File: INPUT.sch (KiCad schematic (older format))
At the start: 41 parts, among them Q701 MMBF170, SW701 SW_PUSH, SW702 C, SW703 1, SW704 4ghi, SW705 7pqrs, SW706 -, SW707 2abc, SW708 5jkl, SW709 8tuv, SW710 UP, SW711 3def, SW712 6mno, SW713 9wxyz, SW714 *+, SW715 DOWN, SW716 0space, SW717 #up

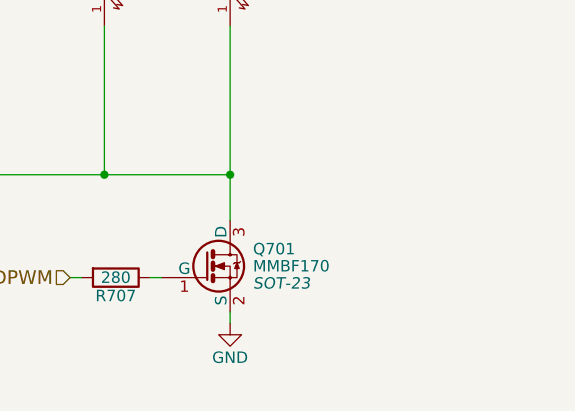
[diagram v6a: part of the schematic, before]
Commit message: Created netlist with current components Foreward Annotation to Board
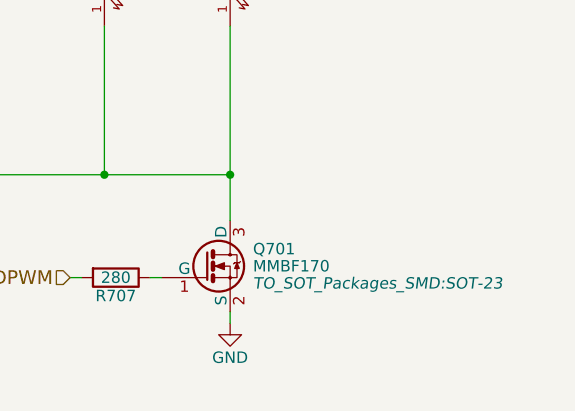
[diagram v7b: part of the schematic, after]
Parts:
- D701, D702, D703, D704, D705, D706: footprint (none) -> LEDs:LED_0603
- Q701: footprint SOT-23 -> TO_SOT_Packages_SMD:SOT-23
- R701, R702, R703, R704, R705, R706, R707, R708: footprint Resistors_SMD:R_0603 -> Resistors_SMD:R_0402
- SW701: footprint buttons:TS-015A -> NokiaRetroFit:TS-015A
- SW702, SW703, SW704, SW705, SW706, SW707, SW708, SW709, SW710, SW711, SW712, SW713, SW714, SW715, SW716, SW717: footprint buttons:Foil_Button -> NokiaRetroFit:Foil_Button
- TP701, TP702, TP703, TP704, TP705, TP706, TP707, TP708, TP709: footprint buttons:TP -> NokiaRetroFit:TP
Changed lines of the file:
@@
 F 0 "SW702" H 2950 3110 50  0000 C CNN
 F 1 "C" H 2800 2921 50  0000 C CNN
-F 2 "buttons:Foil_Button" H 2800 3000 50  0001 C CNN
+F 2 "NokiaRetroFit:Foil_Button" H 2800 3000 50  0001 C CNN
 F 3 "" H 2800 3000 50  0000 C CNN
 	1    2800 3000
@@
 F 0 "SW706" H 3500 3110 50  0000 C CNN
 F 1 "-" H 3350 2921 50  0000 C CNN
-F 2 "buttons:Foil_Button" H 3350 3000 50  0001 C CNN
+F 2 "NokiaRetroFit:Foil_Button" H 3350 3000 50  0001 C CNN
 F 3 "" H 3350 3000 50  0000 C CNN
 	1    3350 3000
@@
 F 0 "SW710" H 4050 3110 50  0000 C CNN
 F 1 "UP" H 3900 2921 50  0000 C CNN
-F 2 "buttons:Foil_Button" H 3900 3000 50  0001 C CNN
+F 2 "NokiaRetroFit:Foil_Button" H 3900 3000 50  0001 C CNN
 F 3 "" H 3900 3000 50  0000 C CNN
 	1    3900 3000
@@
 F 0 "SW715" H 4600 3710 50  0000 C CNN
 F 1 "DOWN" H 4450 3521 50  0000 C CNN
-F 2 "buttons:Foil_Button" H 4450 3600 50  0001 C CNN
+F 2 "NokiaRetroFit:Foil_Button" H 4450 3600 50  0001 C CNN
 F 3 "" H 4450 3600 50  0000 C CNN
 	1    4450 3600
@@
 F 0 "SW703" H 2950 3710 50  0000 C CNN
 F 1 "1" H 2800 3521 50  0000 C CNN
-F 2 "buttons:Foil_Button" H 2800 3600 50  0001 C CNN
+F 2 "NokiaRetroFit:Foil_Button" H 2800 3600 50  0001 C CNN
 F 3 "" H 2800 3600 50  0000 C CNN
 	1    2800 3600
@@
 F 0 "SW707" H 3500 3710 50  0000 C CNN
 F 1 "2abc" H 3350 3521 50  0000 C CNN
-F 2 "buttons:Foil_Button" H 3350 3600 50  0001 C CNN
+F 2 "NokiaRetroFit:Foil_Button" H 3350 3600 50  0001 C CNN
 F 3 "" H 3350 3600 50  0000 C CNN
 	1    3350 3600
@@
 F 0 "SW711" H 4050 3710 50  0000 C CNN
 F 1 "3def" H 3900 3521 50  0000 C CNN
-F 2 "buttons:Foil_Button" H 3900 3600 50  0001 C CNN
+F 2 "NokiaRetroFit:Foil_Button" H 3900 3600 50  0001 C CNN
 F 3 "" H 3900 3600 50  0000 C CNN
 	1    3900 3600
@@
 F 0 "SW704" H 2950 4310 50  0000 C CNN
 F 1 "4ghi" H 2800 4121 50  0000 C CNN
-F 2 "buttons:Foil_Button" H 2800 4200 50  0001 C CNN
+F 2 "NokiaRetroFit:Foil_Button" H 2800 4200 50  0001 C CNN
 F 3 "" H 2800 4200 50  0000 C CNN
 	1    2800 4200
@@
 F 0 "SW708" H 3500 4310 50  0000 C CNN
 F 1 "5jkl" H 3350 4121 50  0000 C CNN
-F 2 "buttons:Foil_Button" H 3350 4200 50  0001 C CNN
+F 2 "NokiaRetroFit:Foil_Button" H 3350 4200 50  0001 C CNN
 F 3 "" H 3350 4200 50  0000 C CNN
 	1    3350 4200
@@
 F 0 "SW712" H 4050 4310 50  0000 C CNN
 F 1 "6mno" H 3900 4121 50  0000 C CNN
-F 2 "buttons:Foil_Button" H 3900 4200 50  0001 C CNN
+F 2 "NokiaRetroFit:Foil_Button" H 3900 4200 50  0001 C CNN
 F 3 "" H 3900 4200 50  0000 C CNN
 	1    3900 4200
@@
 F 0 "SW705" H 2950 4910 50  0000 C CNN
 F 1 "7pqrs" H 2800 4721 50  0000 C CNN
-F 2 "buttons:Foil_Button" H 2800 4800 50  0001 C CNN
+F 2 "NokiaRetroFit:Foil_Button" H 2800 4800 50  0001 C CNN
 F 3 "" H 2800 4800 50  0000 C CNN
 	1    2800 4800
@@
 F 0 "SW709" H 3500 4910 50  0000 C CNN
 F 1 "8tuv" H 3350 4721 50  0000 C CNN
-F 2 "buttons:Foil_Button" H 3350 4800 50  0001 C CNN
+F 2 "NokiaRetroFit:Foil_Button" H 3350 4800 50  0001 C CNN
 F 3 "" H 3350 4800 50  0000 C CNN
 	1    3350 4800
@@
 F 0 "SW713" H 4050 4910 50  0000 C CNN
 F 1 "9wxyz" H 3900 4721 50  0000 C CNN
-F 2 "buttons:Foil_Button" H 3900 4800 50  0001 C CNN
+F 2 "NokiaRetroFit:Foil_Button" H 3900 4800 50  0001 C CNN
 F 3 "" H 3900 4800 50  0000 C CNN
 	1    3900 4800
@@
 F 0 "SW714" H 4600 3110 50  0000 C CNN
 F 1 "*+" H 4450 2921 50  0000 C CNN
-F 2 "buttons:Foil_Button" H 4450 3000 50  0001 C CNN
+F 2 "NokiaRetroFit:Foil_Button" H 4450 3000 50  0001 C CNN
 F 3 "" H 4450 3000 50  0000 C CNN
 	1    4450 3000
@@
 F 0 "SW716" H 4600 4310 50  0000 C CNN
 F 1 "0space" H 4450 4121 50  0000 C CNN
-F 2 "buttons:Foil_Button" H 4450 4200 50  0001 C CNN
+F 2 "NokiaRetroFit:Foil_Button" H 4450 4200 50  0001 C CNN
 F 3 "" H 4450 4200 50  0000 C CNN
 	1    4450 4200
@@
 F 0 "SW717" H 4600 4910 50  0000 C CNN
 F 1 "#up" H 4450 4721 50  0000 C CNN
-F 2 "buttons:Foil_Button" H 4450 4800 50  0001 C CNN
+F 2 "NokiaRetroFit:Foil_Button" H 4450 4800 50  0001 C CNN
 F 3 "" H 4450 4800 50  0000 C CNN
 	1    4450 4800
@@
 F 0 "SW701" H 1850 4510 50  0000 C CNN
 F 1 "SW_PUSH" H 1700 4320 50  0000 C CNN
-F 2 "buttons:TS-015A" H 1700 4400 50  0001 C CNN
+F 2 "NokiaRetroFit:TS-015A" H 1700 4400 50  0001 C CNN
 F 3 "" H 1700 4400 50  0000 C CNN
 	1    1700 4400
@@
 F 0 "R701" V 1780 3650 50  0000 C CNN
 F 1 "10k" V 1700 3650 50  0000 C CNN
-F 2 "Resistors_SMD:R_0603" V 1630 3650 50  0001 C CNN
+F 2 "Resistors_SMD:R_0402" V 1630 3650 50  0001 C CNN
 F 3 "" H 1700 3650 50  0000 C CNN
 	1    1700 3650
@@
 F 0 "R702" V 7130 2650 50  0000 C CNN
 F 1 "280" V 7050 2650 50  0000 C CNN
-F 2 "Resistors_SMD:R_0603" V 6980 2650 50  0001 C CNN
+F 2 "Resistors_SMD:R_0402" V 6980 2650 50  0001 C CNN
 F 3 "" H 7050 2650 50  0000 C CNN
 	1    7050 2650
@@
 F 0 "R703" V 7680 2650 50  0000 C CNN
 F 1 "280" V 7600 2650 50  0000 C CNN
-F 2 "Resistors_SMD:R_0603" V 7530 2650 50  0001 C CNN
+F 2 "Resistors_SMD:R_0402" V 7530 2650 50  0001 C CNN
 F 3 "" H 7600 2650 50  0000 C CNN
 	1    7600 2650
@@
 F 0 "R704" V 8230 2650 50  0000 C CNN
 F 1 "280" V 8150 2650 50  0000 C CNN
-F 2 "Resistors_SMD:R_0603" V 8080 2650 50  0001 C CNN
+F 2 "Resistors_SMD:R_0402" V 8080 2650 50  0001 C CNN
 F 3 "" H 8150 2650 50  0000 C CNN
 	1    8150 2650
@@
 F 0 "R705" V 8780 2650 50  0000 C CNN
 F 1 "280" V 8700 2650 50  0000 C CNN
-F 2 "Resistors_SMD:R_0603" V 8630 2650 50  0001 C CNN
+F 2 "Resistors_SMD:R_0402" V 8630 2650 50  0001 C CNN
 F 3 "" H 8700 2650 50  0000 C CNN
 	1    8700 2650
@@
 F 0 "R706" V 9330 2650 50  0000 C CNN
 F 1 "280" V 9250 2650 50  0000 C CNN
-F 2 "Resistors_SMD:R_0603" V 9180 2650 50  0001 C CNN
+F 2 "Resistors_SMD:R_0402" V 9180 2650 50  0001 C CNN
 F 3 "" H 9250 2650 50  0000 C CNN
 	1    9250 2650
@@
 F 0 "R708" V 9880 2650 50  0000 C CNN
 F 1 "280" V 9800 2650 50  0000 C CNN
-F 2 "Resistors_SMD:R_0603" V 9730 2650 50  0001 C CNN
+F 2 "Resistors_SMD:R_0402" V 9730 2650 50  0001 C CNN
 F 3 "" H 9800 2650 50  0000 C CNN
 	1    9800 2650
@@
 F 0 "TP702" H 2650 2790 20  0000 C CNN
 F 1 "TP" H 2650 2700 60  0001 C CNN
-F 2 "buttons:TP" H 2650 2750 60  0001 C CNN
+F 2 "NokiaRetroFit:TP" H 2650 2750 60  0001 C CNN
 F 3 "" H 2650 2750 60  0000 C CNN
 	1    2650 2750
@@
 F 0 "TP703" H 3200 2790 20  0000 C CNN
 F 1 "TP" H 3200 2700 60  0001 C CNN
-F 2 "buttons:TP" H 3200 2750 60  0001 C CNN
+F 2 "NokiaRetroFit:TP" H 3200 2750 60  0001 C CNN
 F 3 "" H 3200 2750 60  0000 C CNN
 	1    3200 2750
@@
 F 0 "TP704" H 3750 2790 20  0000 C CNN
 F 1 "TP" H 3750 2700 60  0001 C CNN
-F 2 "buttons:TP" H 3750 2750 60  0001 C CNN
+F 2 "NokiaRetroFit:TP" H 3750 2750 60  0001 C CNN
 F 3 "" H 3750 2750 60  0000 C CNN
 	1    3750 2750
@@
 F 0 "TP705" H 4300 2790 20  0000 C CNN
 F 1 "TP" H 4300 2700 60  0001 C CNN
-F 2 "buttons:TP" H 4300 2750 60  0001 C CNN
+F 2 "NokiaRetroFit:TP" H 4300 2750 60  0001 C CNN
 F 3 "" H 4300 2750 60  0000 C CNN
 	1    4300 2750
@@
 F 0 "TP706" H 4850 3190 20  0000 C CNN
 F 1 "TP" H 4850 3100 60  0001 C CNN
-F 2 "buttons:TP" H 4850 3150 60  0001 C CNN
+F 2 "NokiaRetroFit:TP" H 4850 3150 60  0001 C CNN
 F 3 "" H 4850 3150 60  0000 C CNN
 	1    4850 3150
@@
 F 0 "TP707" H 4850 3790 20  0000 C CNN
 F 1 "TP" H 4850 3700 60  0001 C CNN
-F 2 "buttons:TP" H 4850 3750 60  0001 C CNN
+F 2 "NokiaRetroFit:TP" H 4850 3750 60  0001 C CNN
 F 3 "" H 4850 3750 60  0000 C CNN
 	1    4850 3750
@@
 F 0 "TP708" H 4850 4390 20  0000 C CNN
 F 1 "TP" H 4850 4300 60  0001 C CNN
-F 2 "buttons:TP" H 4850 4350 60  0001 C CNN
+F 2 "NokiaRetroFit:TP" H 4850 4350 60  0001 C CNN
 F 3 "" H 4850 4350 60  0000 C CNN
 	1    4850 4350
@@
 F 0 "TP709" H 4850 4990 20  0000 C CNN
 F 1 "TP" H 4850 4900 60  0001 C CNN
-F 2 "buttons:TP" H 4850 4950 60  0001 C CNN
+F 2 "NokiaRetroFit:TP" H 4850 4950 60  0001 C CNN
 F 3 "" H 4850 4950 60  0000 C CNN
 	1    4850 4950
@@
 F 0 "TP701" H 1700 3990 20  0000 C CNN
 F 1 "TP" H 1700 3900 60  0001 C CNN
-F 2 "buttons:TP" H 1700 3950 60  0001 C CNN
+F 2 "NokiaRetroFit:TP" H 1700 3950 60  0001 C CNN
 F 3 "" H 1700 3950 60  0000 C CNN
 	1    1700 3950
@@
 F 0 "Q701" H 9900 4525 50  0000 L CNN
 F 1 "MMBF170" H 9900 4450 50  0000 L CNN
-F 2 "SOT-23" H 9900 4375 50  0000 L CIN
+F 2 "TO_SOT_Packages_SMD:SOT-23" H 9900 4375 50  0000 L CIN
 F 3 "" H 9700 4450 50  0000 L CNN
 	1    9700 4450
@@
 F 0 "R707" V 9380 4500 50  0000 C CNN
 F 1 "280" V 9300 4500 50  0000 C CNN
-F 2 "Resistors_SMD:R_0603" V 9230 4500 50  0001 C CNN
+F 2 "Resistors_SMD:R_0402" V 9230 4500 50  0001 C CNN
 F 3 "" H 9300 4500 50  0000 C CNN
 	1    9300 4500
@@
 F 0 "D701" H 7050 3300 50  0000 C CNN
 F 1 "LED" H 7050 3100 50  0000 C CNN
-F 2 "" H 7050 3200 50  0000 C CNN
+F 2 "LEDs:LED_0603" H 7050 3200 50  0001 C CNN
 F 3 "" H 7050 3200 50  0000 C CNN
 	1    7050 3200
@@
 F 0 "D702" H 7600 3300 50  0000 C CNN
 F 1 "LED" H 7600 3100 50  0000 C CNN
-F 2 "" H 7600 3200 50  0000 C CNN
+F 2 "LEDs:LED_0603" H 7600 3200 50  0001 C CNN
 F 3 "" H 7600 3200 50  0000 C CNN
 	1    7600 3200
@@
 F 0 "D703" H 8150 3300 50  0000 C CNN
 F 1 "LED" H 8150 3100 50  0000 C CNN
-F 2 "" H 8150 3200 50  0000 C CNN
+F 2 "LEDs:LED_0603" H 8150 3200 50  0001 C CNN
 F 3 "" H 8150 3200 50  0000 C CNN
 	1    8150 3200
@@
 F 0 "D704" H 8700 3300 50  0000 C CNN
 F 1 "LED" H 8700 3100 50  0000 C CNN
-F 2 "" H 8700 3200 50  0000 C CNN
+F 2 "LEDs:LED_0603" H 8700 3200 50  0001 C CNN
 F 3 "" H 8700 3200 50  0000 C CNN
 	1    8700 3200
@@
 F 0 "D705" H 9250 3300 50  0000 C CNN
 F 1 "LED" H 9250 3100 50  0000 C CNN
-F 2 "" H 9250 3200 50  0000 C CNN
+F 2 "LEDs:LED_0603" H 9250 3200 50  0001 C CNN
 F 3 "" H 9250 3200 50  0000 C CNN
 	1    9250 3200
@@
 F 0 "D706" H 9800 3300 50  0000 C CNN
 F 1 "LED" H 9800 3100 50  0000 C CNN
-F 2 "" H 9800 3200 50  0000 C CNN
+F 2 "LEDs:LED_0603" H 9800 3200 50  0001 C CNN
 F 3 "" H 9800 3200 50  0000 C CNN
 	1    9800 3200
